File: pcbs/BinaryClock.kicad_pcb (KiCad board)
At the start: 2 copper layers, 76.2 x 50.8 mm, 90 parts, among them IC1 ATTINY2313A-S, P1 USB_OTG, P2 CONN_02X03, Q1 DMG9933USD, Q2 DMG9933USD, Q3 DMG9933USD, SW1 SW_PUSH, U1 FT230XS, U2 STP16CPC26, U3 DS3231M

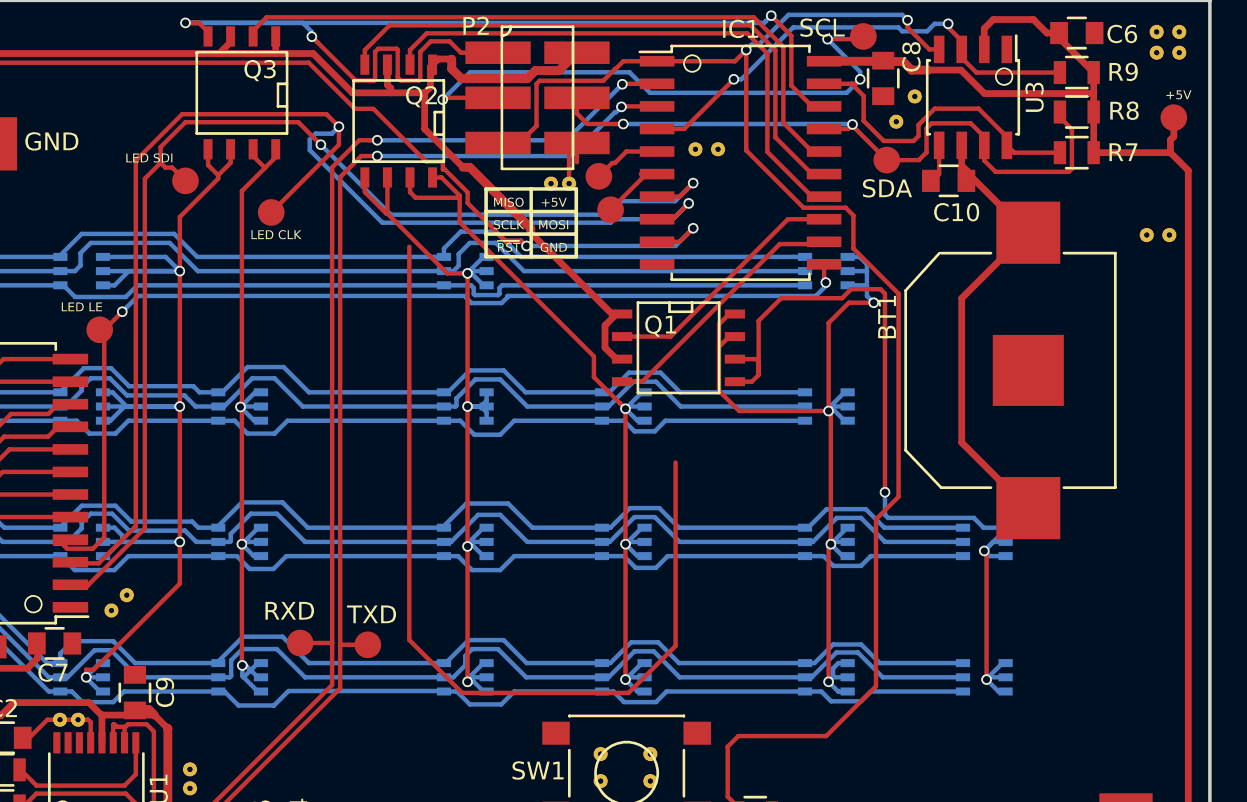
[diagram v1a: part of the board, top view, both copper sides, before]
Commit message: Refactored based on the UART start byte and what it returns
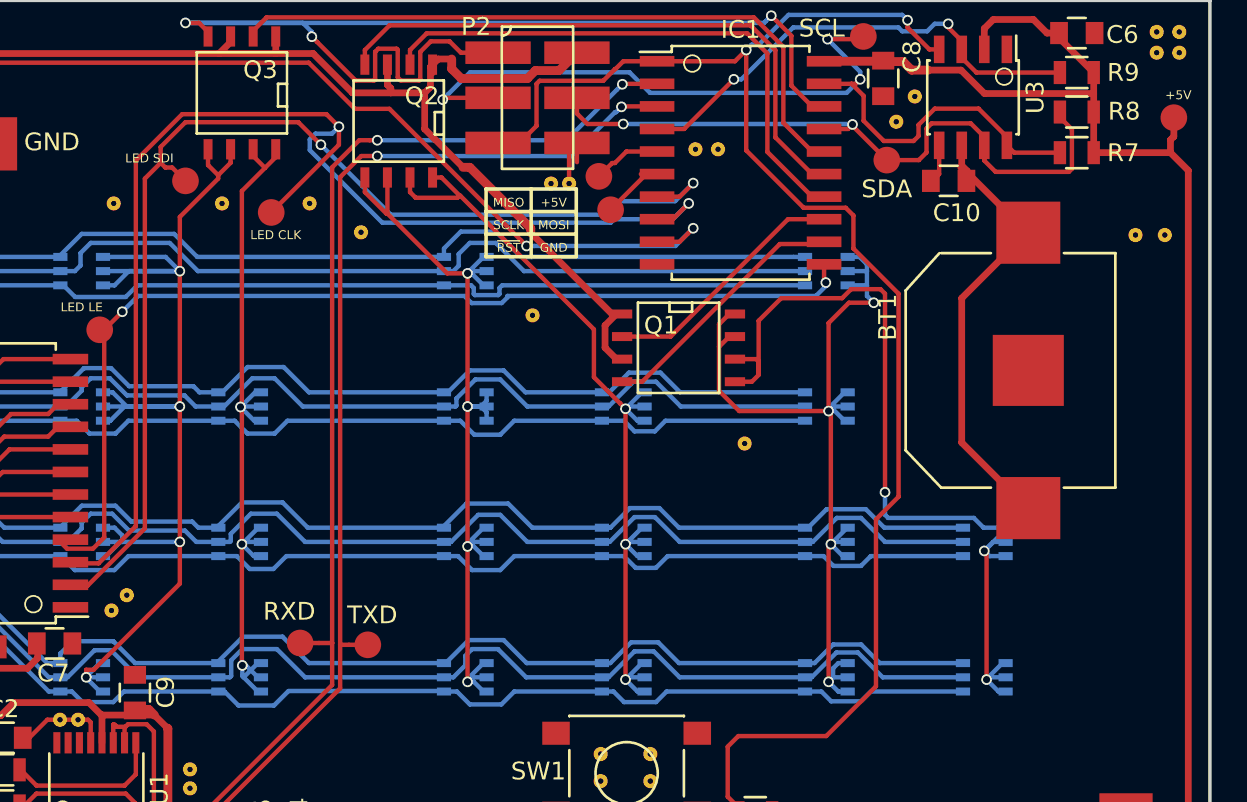
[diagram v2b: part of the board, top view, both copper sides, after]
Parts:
- added REF**: via-0.6mm, TylerCustom:via-0.6mm, F.Cu at (151.6, 126.5)
- added REF**: via-0.6mm, TylerCustom:via-0.6mm, F.Cu at (139.7, 119.3)
- added REF**: via-0.6mm, TylerCustom:via-0.6mm, F.Cu at (116.1, 113.0)
- added REF**: via-0.6mm, TylerCustom:via-0.6mm, F.Cu at (122.2, 113.0)
- added REF**: via-0.6mm, TylerCustom:via-0.6mm, F.Cu at (127.1, 113.0)
- added REF**: via-0.6mm, TylerCustom:via-0.6mm, F.Cu at (130.0, 114.7)
- moved REF** 0.63 mm to (173.6, 114.8)
- moved REF** 0.25 mm to (175.3, 114.8)
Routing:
- net (no net): track 49.8 -> 0.00 mm
- net ~LEDDRV_OE: track 81.8 -> 81.2 mm
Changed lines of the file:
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@@
   (general
     (links 253)
-    (no_connects 1)
+    (no_connects 0)
     (area 101.148999 100.657 180.487085 152.563181)
     (thickness 1.6)
     (drawings 33)
-    (tracks 1156)
+    (tracks 1143)
     (zones 0)
-    (modules 90)
+    (modules 96)
     (nets 60)
   )
@@
   )
   (module TylerCustom:via-0.6mm (layer F.Cu)
+    (at 151.6126 126.5428)
+    (fp_text reference REF** (at 0.05 1.3) (layer F.SilkS) hide
+      (effects (font (size 1 1) (thickness 0.15)))
+    )
+    (fp_text value via-0.6mm (at 0 -1.45) (layer F.Fab) hide
+      (effects (font (size 1 1) (thickness 0.15)))
+    )
+    (pad 1 thru_hole circle (at 0 0) (size 0.8 0.8) (drill 0.3) (layers *.Cu)
+      (net 2 GND) (zone_connect 2))
+  )
+  (module TylerCustom:via-0.6mm (layer F.Cu)
+    (at 139.6746 119.3292)
+    (fp_text reference REF** (at 0.05 1.3) (layer F.SilkS) hide
+      (effects (font (size 1 1) (thickness 0.15)))
+    )
+    (fp_text value via-0.6mm (at 0 -1.45) (layer F.Fab) hide
+      (effects (font (size 1 1) (thickness 0.15)))
+    )
+    (pad 1 thru_hole circle (at 0 0) (size 0.8 0.8) (drill 0.3) (layers *.Cu)
+      (net 2 GND) (zone_connect 2))
+  )
+  (module TylerCustom:via-0.6mm (layer F.Cu)
+    (at 116.1034 113.03)
+    (fp_text reference REF** (at 0.05 1.3) (layer F.SilkS) hide
+      (effects (font (size 1 1) (thickness 0.15)))
+    )
+    (fp_text value via-0.6mm (at 0 -1.45) (layer F.Fab) hide
+      (effects (font (size 1 1) (thickness 0.15)))
+    )
+    (pad 1 thru_hole circle (at 0 0) (size 0.8 0.8) (drill 0.3) (layers *.Cu)
+      (net 2 GND) (zone_connect 2))
+  )
+  (module TylerCustom:via-0.6mm (layer F.Cu)
+    (at 122.1994 113.03)
+    (fp_text reference REF** (at 0.05 1.3) (layer F.SilkS) hide
+      (effects (font (size 1 1) (thickness 0.15)))
+    )
+    (fp_text value via-0.6mm (at 0 -1.45) (layer F.Fab) hide
+      (effects (font (size 1 1) (thickness 0.15)))
+    )
+    (pad 1 thru_hole circle (at 0 0) (size 0.8 0.8) (drill 0.3) (layers *.Cu)
+      (net 2 GND) (zone_connect 2))
+  )
+  (module TylerCustom:via-0.6mm (layer F.Cu)
+    (at 127.127 113.03)
+    (fp_text reference REF** (at 0.05 1.3) (layer F.SilkS) hide
+      (effects (font (size 1 1) (thickness 0.15)))
+    )
+    (fp_text value via-0.6mm (at 0 -1.45) (layer F.Fab) hide
+      (effects (font (size 1 1) (thickness 0.15)))
+    )
+    (pad 1 thru_hole circle (at 0 0) (size 0.8 0.8) (drill 0.3) (layers *.Cu)
+      (net 2 GND) (zone_connect 2))
+  )
+  (module TylerCustom:via-0.6mm (layer F.Cu)
+    (at 130.0226 114.6556)
+    (fp_text reference REF** (at 0.05 1.3) (layer F.SilkS) hide
+      (effects (font (size 1 1) (thickness 0.15)))
+    )
+    (fp_text value via-0.6mm (at 0 -1.45) (layer F.Fab) hide
+      (effects (font (size 1 1) (thickness 0.15)))
+    )
+    (pad 1 thru_hole circle (at 0 0) (size 0.8 0.8) (drill 0.3) (layers *.Cu)
+      (net 2 GND) (zone_connect 2))
+  )
+  (module TylerCustom:via-0.6mm (layer F.Cu)
     (at 176.0728 104.5464)
     (fp_text reference REF** (at 0.05 1.3) (layer F.SilkS) hide
@@
   )
   (module TylerCustom:via-0.6mm (layer F.Cu)
-    (at 175.514 114.808)
+    (at 175.26 114.808)
     (fp_text reference REF** (at 0.05 1.3) (layer F.SilkS) hide
       (effects (font (size 1 1) (thickness 0.15)))
@@
   )
   (module TylerCustom:via-0.6mm (layer F.Cu)
-    (at 174.244 114.808)
+    (at 173.609 114.808)
     (fp_text reference REF** (at 0.05 1.3) (layer F.SilkS) hide
       (effects (font (size 1 1) (thickness 0.15)))
@@
   (gr_line (start 177.8 152.4) (end 177.8 101.6) (angle 90) (layer Edge.Cuts) (width 0.2))
   (gr_line (start 101.6 152.4) (end 177.8 152.4) (angle 90) (layer Edge.Cuts) (width 0.2))
-  (segment (start 147.7264 127.6096) (end 147.7264 137.932602) (width 0.25) (layer F.Cu) (net 0))
-  (segment (start 147.7264 137.932602) (end 145.080003 140.578999) (width 0.25) (layer F.Cu) (net 0))
-  (segment (start 145.080003 140.578999) (end 135.716999 140.578999) (width 0.25) (layer F.Cu) (net 0))
-  (segment (start 135.716999 140.578999) (end 132.7404 137.6024) (width 0.25) (layer F.Cu) (net 0))
-  (segment (start 132.7404 137.6024) (end 132.7404 115.46981) (width 0.25) (layer F.Cu) (net 0))
   (segment (start 156.084 105.029) (end 159.3756 105.029) (width 0.5) (layer F.Cu) (net 1))
   (segment (start 159.3756 105.029) (end 159.4104 104.9942) (width 0.5) (layer F.Cu) (net 1))
@@
   (segment (start 155.956 115.316) (end 156.083 115.189) (width 0.25) (layer F.Cu) (net 10) (status 30))
   (segment (start 156.083 115.189) (end 156.084 115.189) (width 0.25) (layer F.Cu) (net 10) (status 30))
-  (segment (start 135.5725 112.5895) (end 135.5725 114.0841) (width 0.25) (layer F.Cu) (net 11))
-  (segment (start 135.5725 114.0841) (end 143.129 121.6406) (width 0.25) (layer F.Cu) (net 11))
-  (segment (start 143.129 121.6406) (end 143.129 122.809) (width 0.25) (layer F.Cu) (net 11))
-  (segment (start 143.129 122.809) (end 144.606995 124.286995) (width 0.25) (layer F.Cu) (net 11))
-  (segment (start 144.606995 124.286995) (end 144.607001 124.286995) (width 0.25) (layer F.Cu) (net 11))
+  (segment (start 135.6019 112.5895) (end 143.129 120.1166) (width 0.25) (layer F.Cu) (net 11))
   (segment (start 144.607001 124.286995) (end 144.907 124.586994) (width 0.25) (layer F.Cu) (net 11))
+  (segment (start 144.606995 124.286995) (end 144.607001 124.286995) (width 0.25) (layer F.Cu) (net 11))
+  (segment (start 135.5725 112.5895) (end 135.6019 112.5895) (width 0.25) (layer F.Cu) (net 11))
+  (segment (start 143.129 120.1166) (end 143.129 122.809) (width 0.25) (layer F.Cu) (net 11))
+  (segment (start 143.129 122.809) (end 144.606995 124.286995) (width 0.25) (layer F.Cu) (net 11))
+  (segment (start 145.98 139.7) (end 145.034 139.7) (width 0.25) (layer B.Cu) (net 11) (status 10))
   (segment (start 145.98 123.66) (end 145.833994 123.66) (width 0.25) (layer B.Cu) (net 11) (status 30))
   (segment (start 145.833994 123.66) (end 144.907 124.586994) (width 0.25) (layer B.Cu) (net 11) (status 10))
@@
   (segment (start 145.98 138.9) (end 145.834 138.9) (width 0.25) (layer B.Cu) (net 11) (status 30))
   (segment (start 145.834 138.9) (end 144.907 139.827) (width 0.25) (layer B.Cu) (net 11) (status 10))
-  (segment (start 145.98 139.7) (end 145.034 139.7) (width 0.25) (layer B.Cu) (net 11) (status 10))
   (segment (start 145.034 139.7) (end 144.907 139.827) (width 0.25) (layer B.Cu) (net 11))
   (segment (start 145.98 140.5) (end 145.58 140.5) (width 0.25) (layer B.Cu) (net 11) (status 30))
@@
   (segment (start 104.3295 134.5565) (end 104.266 134.493) (width 0.25) (layer F.Cu) (net 45) (status 30))
   (segment (start 105.8545 134.5565) (end 104.3295 134.5565) (width 0.25) (layer F.Cu) (net 45) (status 20))
+  (segment (start 139.038736 115.123266) (end 139.338735 115.423265) (width 0.25) (layer F.Cu) (net 47))
+  (segment (start 131.621468 107.705998) (end 139.038736 115.123266) (width 0.25) (layer F.Cu) (net 47))
+  (segment (start 127.080511 105.109511) (end 129.676998 107.705998) (width 0.25) (layer F.Cu) (net 47))
+  (segment (start 105.710489 105.109511) (end 127.080511 105.109511) (width 0.25) (layer F.Cu) (net 47))
+  (segment (start 103.124 107.696) (end 105.710489 105.109511) (width 0.25) (layer F.Cu) (net 47))
+  (segment (start 129.676998 107.705998) (end 131.621468 107.705998) (width 0.25) (layer F.Cu) (net 47))
   (segment (start 103.566 131.953) (end 104.266 131.953) (width 0.25) (layer F.Cu) (net 47))
   (segment (start 102.928311 131.315311) (end 103.566 131.953) (width 0.25) (layer F.Cu) (net 47))
   (segment (start 102.928311 107.891689) (end 102.928311 131.315311) (width 0.25) (layer F.Cu) (net 47))
   (segment (start 103.124 107.696) (end 102.928311 107.891689) (width 0.25) (layer F.Cu) (net 47))
-  (segment (start 103.124 107.696) (end 105.710489 105.109511) (width 0.25) (layer F.Cu) (net 47))
-  (segment (start 105.710489 105.109511) (end 127.080511 105.109511) (width 0.25) (layer F.Cu) (net 47))
-  (segment (start 134.738901 111.119491) (end 136.02251 112.4031) (width 0.25) (layer F.Cu) (net 47))
-  (segment (start 127.080511 105.109511) (end 129.676998 107.705998) (width 0.25) (layer F.Cu) (net 47))
-  (segment (start 129.676998 107.705998) (end 130.718398 107.705998) (width 0.25) (layer F.Cu) (net 47))
-  (segment (start 130.718398 107.705998) (end 133.685399 110.672999) (width 0.25) (layer F.Cu) (net 47))
-  (segment (start 134.627501 110.737999) (end 134.627501 111.11949) (width 0.25) (layer F.Cu) (net 47))
-  (segment (start 133.685399 110.672999) (end 134.562501 110.672999) (width 0.25) (layer F.Cu) (net 47))
-  (segment (start 134.562501 110.672999) (end 134.627501 110.737999) (width 0.25) (layer F.Cu) (net 47))
-  (segment (start 134.627501 111.11949) (end 134.738901 111.119491) (width 0.25) (layer F.Cu) (net 47))
-  (segment (start 136.02251 112.4031) (end 136.02251 113.01011) (width 0.25) (layer F.Cu) (net 47))
-  (segment (start 136.02251 113.01011) (end 138.135666 115.123266) (width 0.25) (layer F.Cu) (net 47))
-  (segment (start 138.135666 115.123266) (end 139.038736 115.123266) (width 0.25) (layer F.Cu) (net 47))
-  (segment (start 139.038736 115.123266) (end 139.338735 115.423265) (width 0.25) (layer F.Cu) (net 47))
   (segment (start 147.720735 115.423265) (end 139.762999 115.423265) (width 0.25) (layer B.Cu) (net 47))
   (segment (start 139.762999 115.423265) (end 139.338735 115.423265) (width 0.25) (layer B.Cu) (net 47))

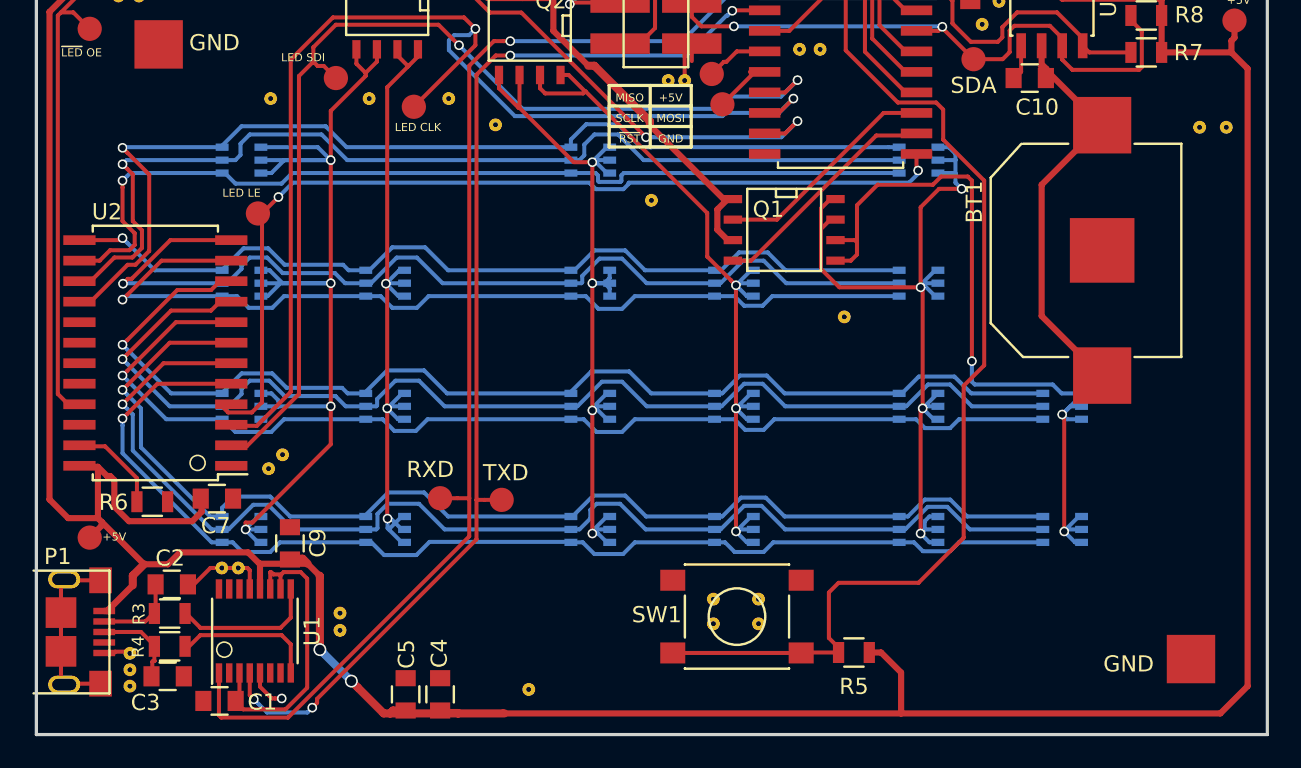
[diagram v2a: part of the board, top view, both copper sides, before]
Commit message: Saving clock color and fixing the GUI
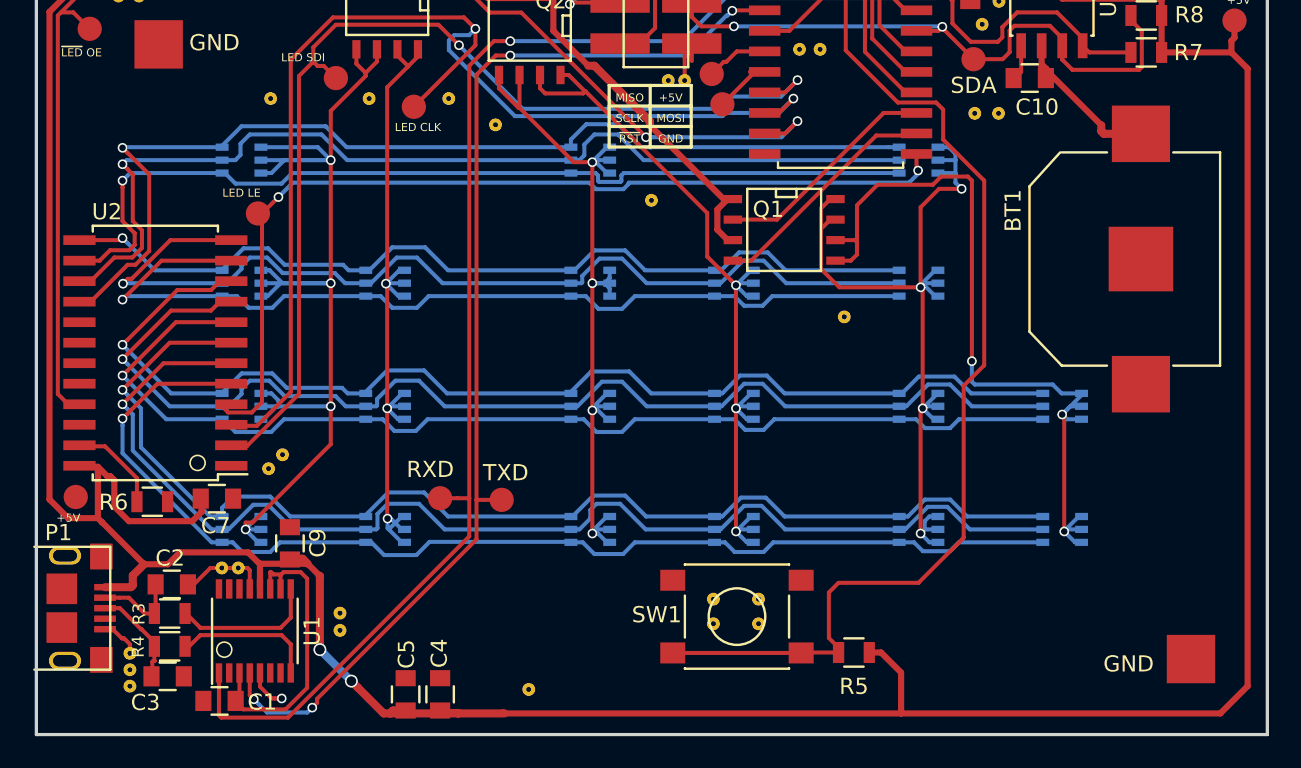
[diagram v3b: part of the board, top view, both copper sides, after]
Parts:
- moved REF** 14.1 mm to (161.2, 113.9)
- moved REF** 13.9 mm to (159.7, 113.9)
- moved W2 2.66 mm to (104.0, 137.7)
- moved BT1 2.46 mm to (170.0, 123.0)
- moved P1 1.47 mm to (103.2, 144.6)
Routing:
- net +BATT: track 27.1 -> 10.2 mm
- net Net-(P1-Pad6): track 11.5 -> 0.00 mm
- net +5V: track 289.7 -> 287.8 mm
- net Net-(C3-Pad1): track 5.79 -> 6.53 mm

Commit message: making some minor formatting changes
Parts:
- removed the REF** at (151.6, 126.5)
- added REF**: via-0.6mm, TylerCustom:via-0.6mm, F.Cu at (142.8, 127.9)
- added REF**: via-0.6mm, TylerCustom:via-0.6mm, F.Cu at (110.9, 134.7)
- added REF**: via-0.6mm, TylerCustom:via-0.6mm, F.Cu at (129.1, 149.6)
- added REF**: via-0.6mm, TylerCustom:via-0.6mm, F.Cu at (130.7, 149.6)
- added REF**: via-0.6mm, TylerCustom:via-0.6mm, F.Cu at (172.1, 144.4)
- added REF**: via-0.6mm, TylerCustom:via-0.6mm, F.Cu at (174.1, 144.4)
- added REF**: via-0.6mm, TylerCustom:via-0.6mm, F.Cu at (161.2, 115.4)
- added REF**: via-0.6mm, TylerCustom:via-0.6mm, F.Cu at (159.7, 115.3)
- added REF**: via-0.6mm, TylerCustom:via-0.6mm, F.Cu at (140.6, 127.9)
- added REF**: via-0.6mm, TylerCustom:via-0.6mm, F.Cu at (138.1, 127.9)
- added REF**: via-0.6mm, TylerCustom:via-0.6mm, F.Cu at (132.3, 127.9)
- added REF**: via-0.6mm, TylerCustom:via-0.6mm, F.Cu at (134.1, 127.9)
- added REF**: via-0.6mm, TylerCustom:via-0.6mm, F.Cu at (130.4, 127.9)
- added REF**: via-0.6mm, TylerCustom:via-0.6mm, F.Cu at (126.9, 127.9)
- added REF**: via-0.6mm, TylerCustom:via-0.6mm, F.Cu at (124.8, 127.9)
- added REF**: via-0.6mm, TylerCustom:via-0.6mm, F.Cu at (121.6, 127.9)
- moved REF** 0.45 mm to (120.7, 144.6)
- moved REF** 0.31 mm to (120.7, 145.9)
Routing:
- net +BATT: track 10.2 -> 9.49 mm
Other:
- board text added: "Binary Clock v2.1 Tyler Holmes 7/2017"
